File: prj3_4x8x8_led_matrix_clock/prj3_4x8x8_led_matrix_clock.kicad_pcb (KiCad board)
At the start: 2 copper layers, 133.4 x 53.3 mm, 19 parts, among them J1 Barrel_Jack, J2 LED1_IN, J3 LED1_OUT, J4 LED2_IN, J5 LED2_OUT, J6 LED3_IN, J7 LED3_OUT, J8 LED4_IN, J9 LED4_OUT, U1 ArduinoProMini_FG

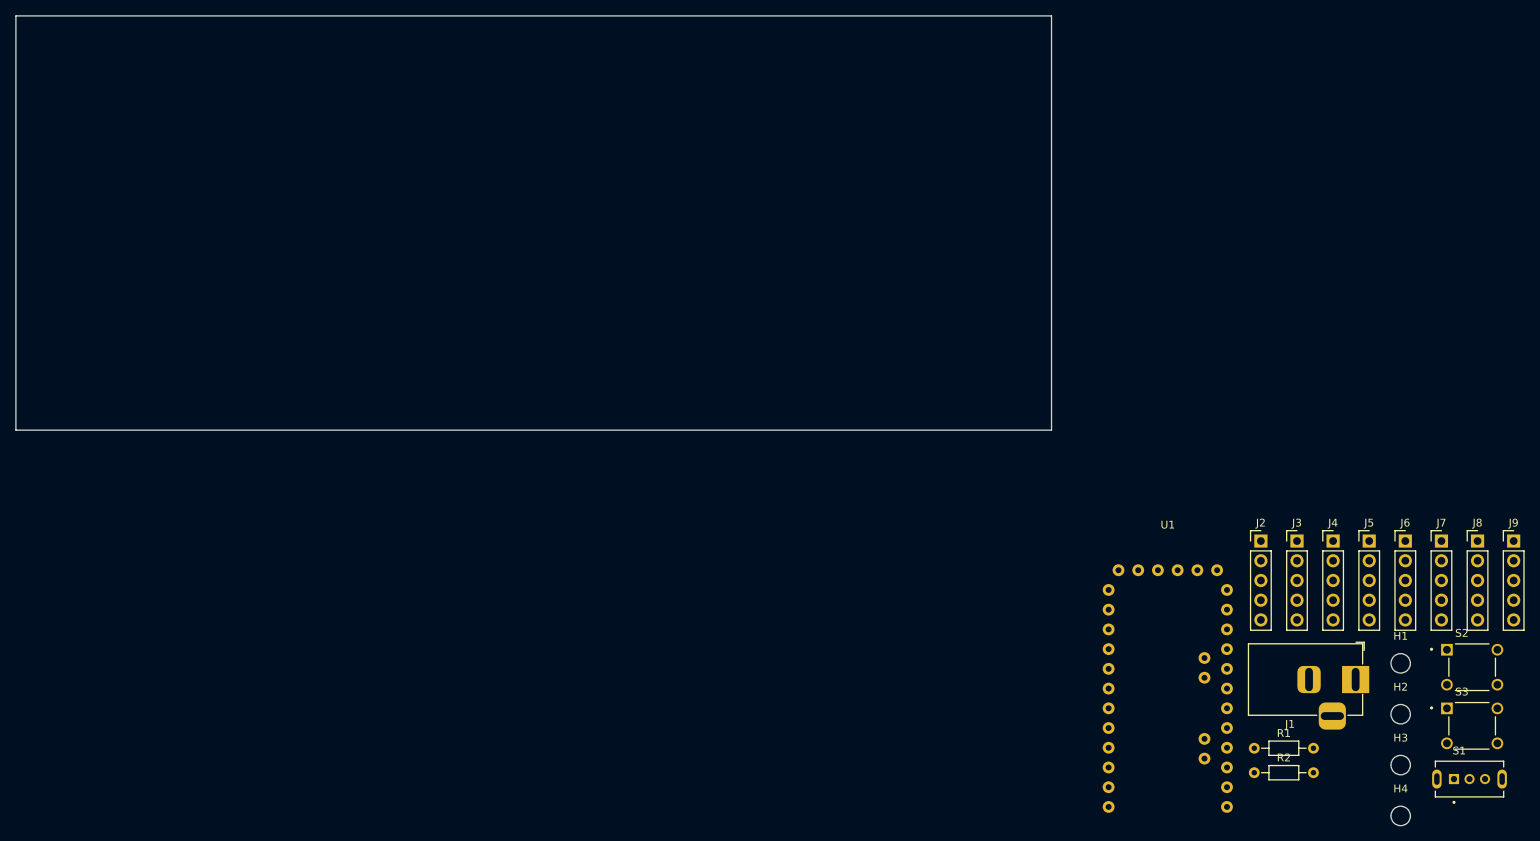
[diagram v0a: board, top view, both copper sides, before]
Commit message: Concluso posizionamento e bordi PCB progetto 3
Feat: sistemati i bordi della scheda
Feat: posizionati i footprint sul PCB
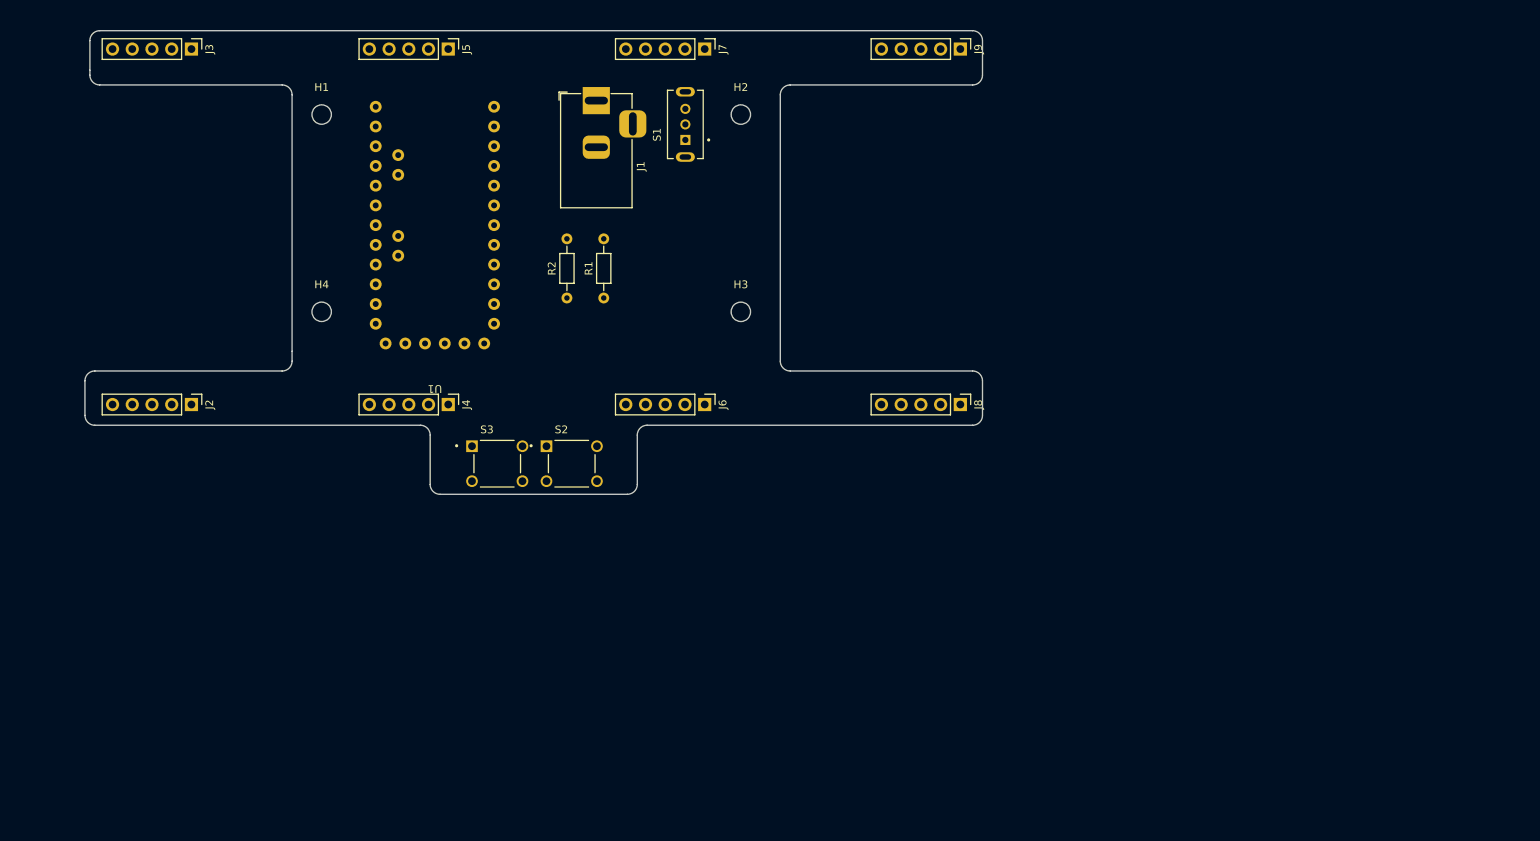
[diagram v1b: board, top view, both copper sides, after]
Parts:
- moved H1 155.9 mm to (118.1, 58.4)
- moved J3 155.8 mm to (101.3, 50.0), turned to -90 degrees
- moved H4 153.4 mm to (118.1, 83.8)
- moved J2 138.8 mm to (101.3, 95.8), turned to -90 degrees
- moved J5 134.4 mm to (134.4, 50.0), turned to -90 degrees
- moved S1 131.5 mm to (164.9, 59.7), turned to 90 degrees
- moved S3 130.0 mm to (140.7, 103.4)
- moved J1 123.0 mm to (153.5, 56.6), turned to 90 degrees
- moved S2 118.9 mm to (150.3, 103.4)
- moved J4 115.3 mm to (134.4, 95.8), turned to -90 degrees
- moved H2 114.8 mm to (172.1, 58.4)
- moved J7 114.1 mm to (167.4, 50.0), turned to -90 degrees
- moved R2 107.6 mm to (149.7, 82.0), turned to 90 degrees
- moved H3 103.1 mm to (172.1, 83.8)
- moved R1 101.9 mm to (154.4, 82.0), turned to 90 degrees
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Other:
- board size 133.4 x 53.3 mm -> 115.6 x 59.7 mm

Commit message: Spostati alcuni componenti nel retro del PCB
Feat: spostati U1, R1, R2, J1, S1 nel retro
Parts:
- J1, R1, R2, S1, U1: moved to B.Cu
- moved S1 0.47 mm to (164.5, 59.7)
- turned U1 to 0 degrees

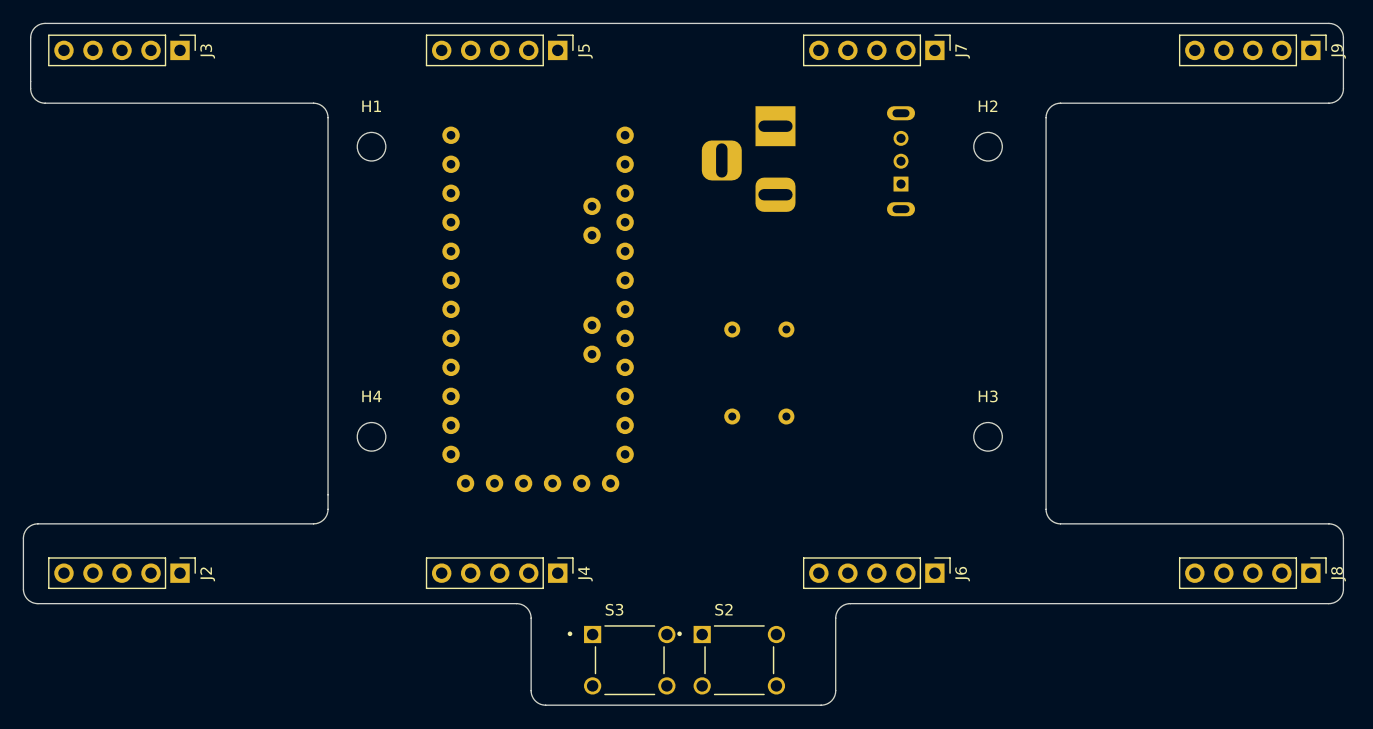
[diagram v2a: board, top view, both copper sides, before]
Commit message: Completamento tracce progetto 3
Feat: create tracce per i segnali
Feat: create filled zone per Vcc e GND
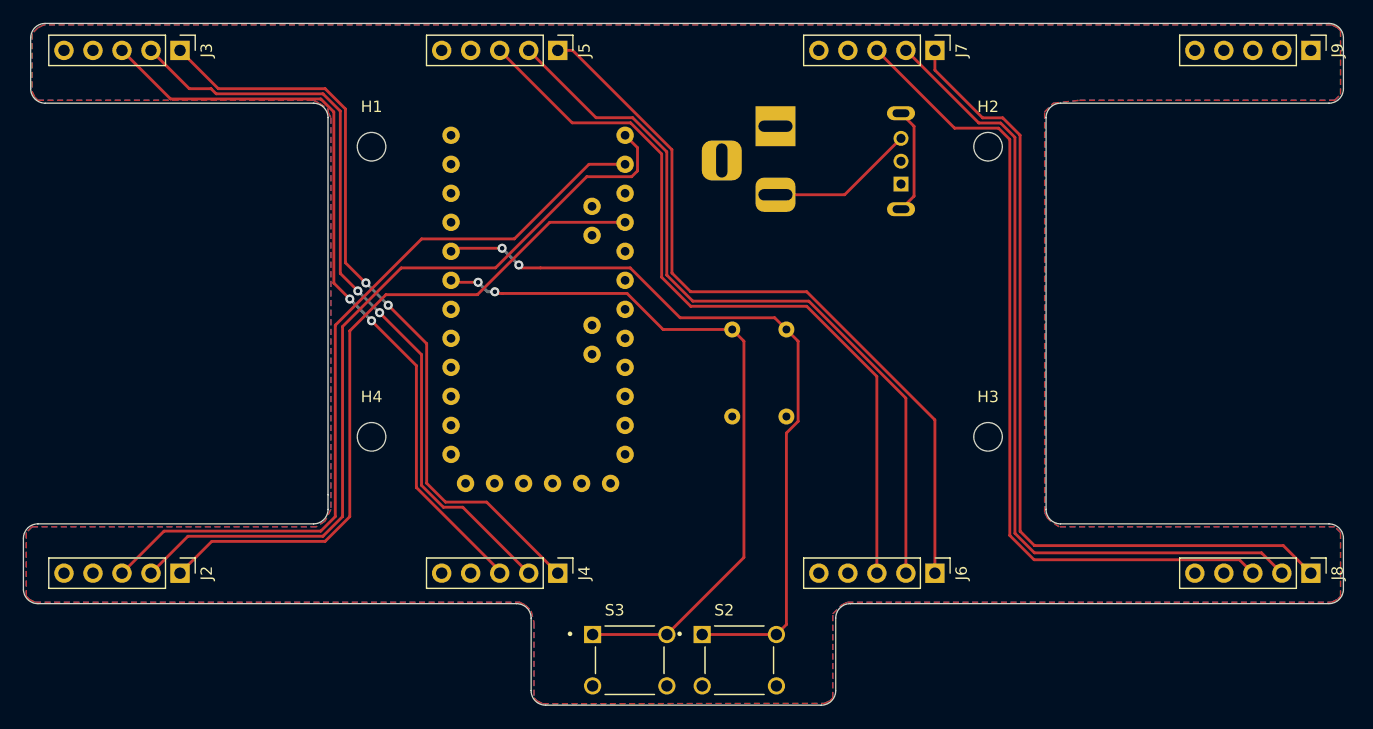
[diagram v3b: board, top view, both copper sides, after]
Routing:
- net /CIN3: track 0.00 -> 73.2 mm
- net /DIN3: track 0.00 -> 72.2 mm
- net /CLK3: track 0.00 -> 72.2 mm
- net /DIN0: track 0.00 -> 70.5 mm
- net /CLK0: track 0.00 -> 68.7 mm
- net /CLK2: track 0.00 -> 68.4 mm
- net /DIN2: track 0.00 -> 67.3 mm
- net /CLK1: track 0.00 -> 67.2 mm, vias 0 -> 2
- net /CIN1: track 0.00 -> 67.1 mm, vias 0 -> 2
- net /DIN1: track 0.00 -> 67.1 mm, vias 0 -> 2
- net /TIMER_RESET: track 0.00 -> 66.8 mm, vias 0 -> 2
- net /CIN2: track 0.00 -> 66.2 mm
- net /MODE_SELECT: track 0.00 -> 62.8 mm, vias 0 -> 2
- net /CIN0: track 0.00 -> 61.2 mm
- net Net-(J1-Pad2): track 0.00 -> 13.0 mm
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- added copper zone on F.Cu, net /Vcc
- added copper zone on B.Cu, net GND

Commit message: Ultimi ritocchi progetto 3 e correzioni
Feat: aggiunte/aggiustate varie silkscreen
Feat: aggiunti modelli 3D mancanti
Fix: corretti nomi dei net nello schematico e nel PCB
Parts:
- added REF**: KiCad-Logo2_5mm_SilkScreen, Symbol:KiCad-Logo2_5mm_SilkScreen, B.Cu at (145.5, 51.1)
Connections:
- J2 pad 1: /CIN0 -> /CLK0
- J2 pad 2: /DIN0 -> /CS0
- J2 pad 3: /CLK0 -> /DIN0
- J3 pad 1: /CIN1 -> /CLK1
- J3 pad 2: /DIN1 -> /CS1
- J3 pad 3: /CLK1 -> /DIN1
- J4 pad 1: /CIN1 -> /CLK1
- J4 pad 2: /DIN1 -> /CS1
- J4 pad 3: /CLK1 -> /DIN1
- J5 pad 1: /CIN2 -> /CLK2
- J5 pad 2: /DIN2 -> /CS2
- J5 pad 3: /CLK2 -> /DIN2
- J6 pad 1: /CIN2 -> /CLK2
- J6 pad 2: /DIN2 -> /CS2
- J6 pad 3: /CLK2 -> /DIN2
- J7 pad 1: /CIN3 -> /CLK3
- J7 pad 2: /DIN3 -> /CS3
- J7 pad 3: /CLK3 -> /DIN3
- J8 pad 1: /CIN3 -> /CLK3
- J8 pad 2: /DIN3 -> /CS3
- J8 pad 3: /CLK3 -> /DIN3
- U1 pad 17: /DIN0 -> /CS0
- U1 pad 6: /CIN0 -> /CLK0
- U1 pad 8: /CLK0 -> /DIN0
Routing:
- net /CIN3: track 73.2 -> 0.00 mm
- net /CS3: track 0.00 -> 72.2 mm
- net /CS0: track 0.00 -> 70.5 mm
- net /CS2: track 0.00 -> 67.3 mm
- net /CIN1: track 67.1 -> 0.00 mm, vias 2 -> 0
- net /CS1: track 0.00 -> 67.1 mm, vias 0 -> 2
- net /CIN2: track 66.2 -> 0.00 mm
- net /CIN0: track 61.2 -> 0.00 mm
- net /CLK0: track 68.7 -> 61.2 mm
- net /CLK2: track 68.4 -> 66.2 mm
- net /DIN0: track 70.5 -> 68.7 mm
- net /DIN2: track 67.3 -> 68.4 mm
- net /CLK3: track 72.2 -> 73.2 mm
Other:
- board text added: "0,0000 mm / 0,0000 mm"
- board text added: "0,3000 mm"
- board text added: "1,6000 mm"
- board text added: "115,5700 mm x 59,6900 mm"
- board text added: "2"
- board text added: "4x8x8 LED matrix clock"
- board text added: "BOARD CHARACTERISTICS"
- board text added: "Board Thickness:"
- board text added: "Board overall dimensions:"
- board text added: "Castellated pads:"
- board text added: "Copper Finish:"
- board text added: "Copper Layer Count:"
- board text added: "Edge card connectors:"
- board text added: "Impedance Control:"
- board text added: "Min hole diameter:"
- board text added: "Min track/spacing:"
- board text added: "Mode"
- board text added: "No"
- board text added: "None"
- board text added: "OFF"
- board text added: "ON"
- board text added: "Plated Board Edge:"
- board text added: "Reset"
- board text added: "Version: ${design_version}"
